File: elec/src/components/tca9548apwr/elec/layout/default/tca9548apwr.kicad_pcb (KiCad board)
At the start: 2 copper layers, 20 parts

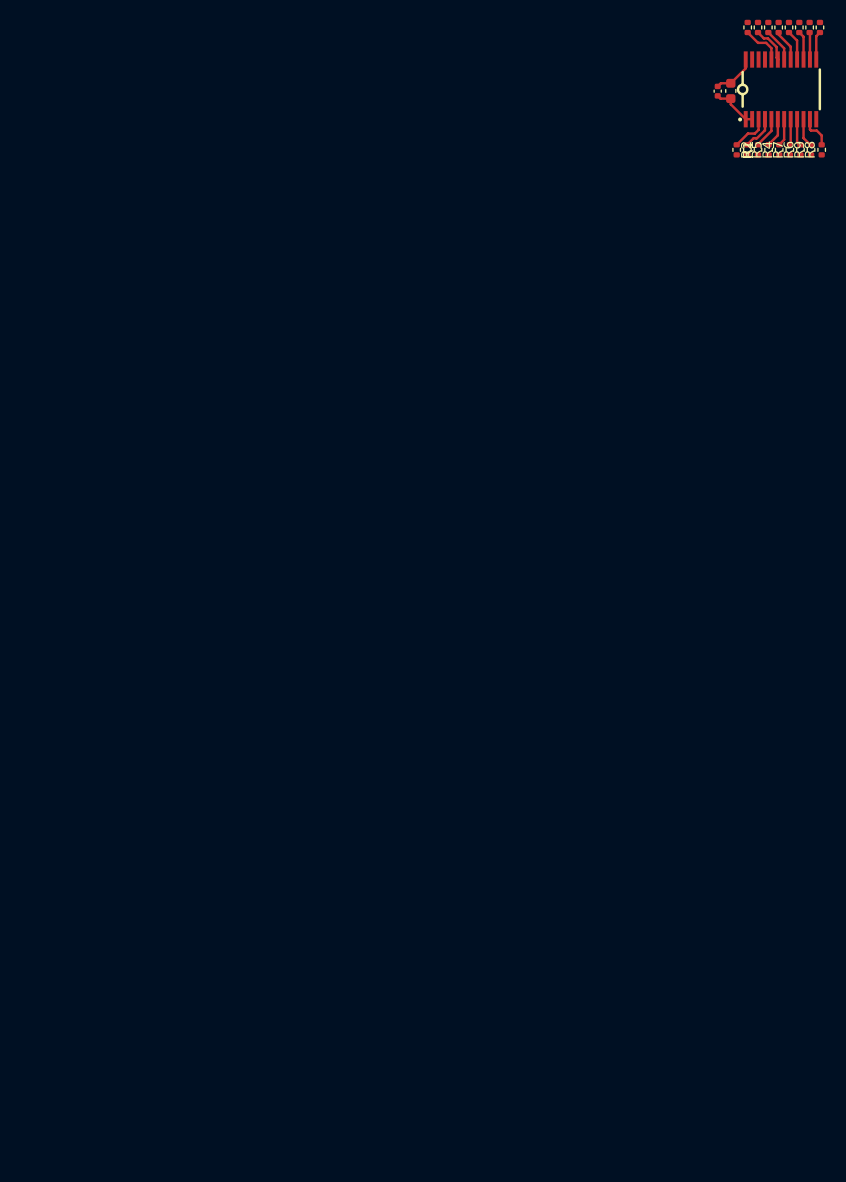
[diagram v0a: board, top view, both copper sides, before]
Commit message: update all value -> resistance/capacitance, update layout for cellsim8ch, nets seem to be broken
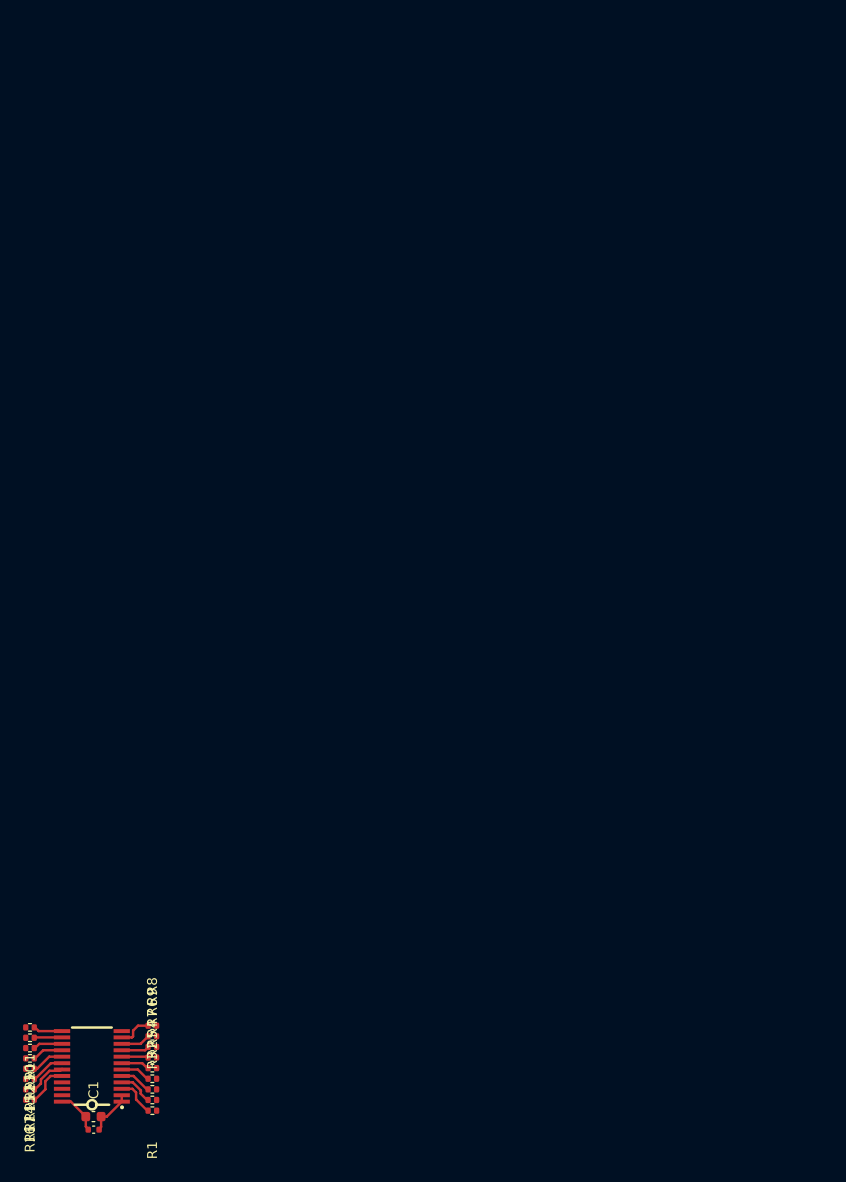
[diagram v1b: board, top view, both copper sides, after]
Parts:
- moved R16 130.5 mm to (122.0, 154.4), turned to 180 degrees
- moved R17 130.3 mm to (122.0, 153.4), turned to 180 degrees
- moved R14 130.0 mm to (122.0, 152.3), turned to 180 degrees
- moved R15 129.8 mm to (122.0, 151.3), turned to 180 degrees
- moved R12 129.5 mm to (122.0, 150.2), turned to 180 degrees
- moved R13 129.3 mm to (122.0, 149.2), turned to 180 degrees
- moved R10 129.1 mm to (122.0, 148.1), turned to 180 degrees
- moved R11 128.9 mm to (122.0, 147.1), turned to 180 degrees
- moved C1 122.6 mm to (128.5, 157.4), turned to 0 degrees
- moved C2 122.2 mm to (128.4, 156.1), turned to 0 degrees
- moved U1 121.0 mm to (128.3, 151.0), turned to 90 degrees
- moved R1 113.8 mm to (134.4, 155.5), turned to 180 degrees
- moved R3 113.4 mm to (134.4, 154.4), turned to 0 degrees
- moved R2 113.1 mm to (134.4, 153.4), turned to 0 degrees
- moved R5 112.8 mm to (134.4, 152.3), turned to 0 degrees
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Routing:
- net ic-scl-7: track 4.21 -> 0.00 mm
- net 35: track 0.00 -> 4.21 mm
- net reset_: track 3.91 -> 0.00 mm
- net ic-sda-7: track 3.89 -> 0.00 mm
- net 32: track 0.00 -> 3.89 mm
- net 27: track 0.00 -> 3.51 mm
- net ic-sda: track 3.51 -> 0.00 mm
- net 22: track 0.00 -> 3.42 mm
- net ic-scl-3: track 3.42 -> 0.00 mm
- net ic-scl-6: track 3.40 -> 0.00 mm
- net 34: track 0.00 -> 3.40 mm
- net 26: track 0.00 -> 3.24 mm
- net ic-sda-6: track 3.24 -> 0.00 mm
- net 36: track 0.00 -> 3.13 mm
- net ic-scl: track 3.13 -> 0.00 mm
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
